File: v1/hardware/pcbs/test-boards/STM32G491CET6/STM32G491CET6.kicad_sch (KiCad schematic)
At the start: 43 parts, among them J1 Conn_02x10_Odd_Even, J2 Conn_02x10_Odd_Even, J3 Conn_01x04, U1 STM32G491CETx, Y1 Crystal_GND24, Y2 Crystal

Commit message: not sure what i did
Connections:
- net +3V3: now also C6.2, U1.1 (VBAT)
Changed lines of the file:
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@@
 	)
 	(junction
+		(at 107.95 54.61)
+		(diameter 0)
+		(color 0 0 0 0)
+	)
+	(junction
 		(at 157.48 54.61)
 		(diameter 0)
@@
 					(unit 1)
 				)
+			)
+		)
+	)
+	(symbol
+		(lib_id "power:+3V3")
+		(at 107.95 54.61 90)
+		(unit 1)
+		(exclude_from_sim no)
+		(in_bom yes)
+		(on_board yes)
+		(dnp no)
+		(fields_autoplaced yes)
+		(property "Reference" "#PWR057"
+			(at 111.76 54.61 0)
+			(effects
+				(font
+					(size 1.27 1.27)
+				)
+				(hide yes)
+			)
+		)
+		(property "Value" "+3V3"
+			(at 104.14 54.61 90)
+			(effects
+				(font
+					(size 1.27 1.27)
+				)
+				(justify left)
+			)
+		)
+		(property "Footprint" ""
+			(at 107.95 54.61 0)
+			(effects
+				(font
+					(size 1.27 1.27)
+				)
+				(hide yes)
+			)
+		)
+		(property "Datasheet" ""
+			(at 107.95 54.61 0)
+			(effects
+				(font
+					(size 1.27 1.27)
+				)
+				(hide yes)
+			)
+		)
+		(property "Description" "Power symbol creates a global label with name \"+3V3\""
+			(at 107.95 54.61 0)
+			(effects
+				(font
+					(size 1.27 1.27)
+				)
+				(hide yes)
+			)
+		)
+		(pin "1"
+		)
+		(instances
+			(project "STM32G491CET6"
+				(path "/ca218c03-4ff0-46e7-9492-03c917b647a9"
+					(reference "#PWR057")
+					(unit 1)
+				)

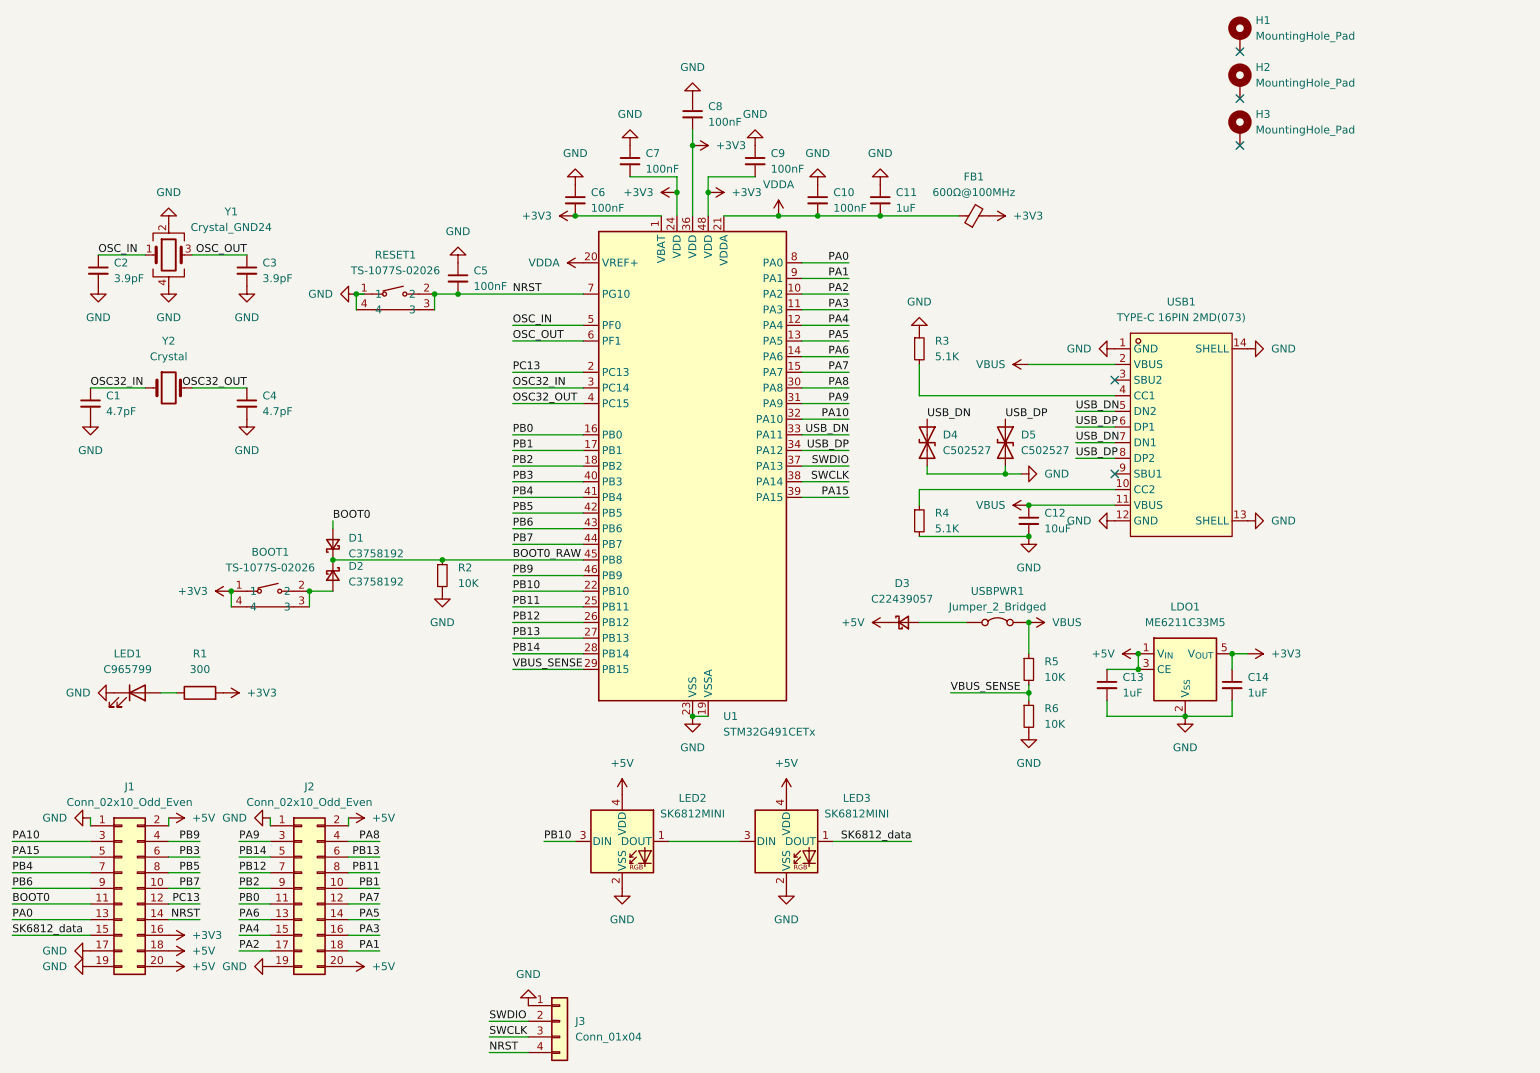
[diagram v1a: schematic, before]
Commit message: fixed STM32G4 breakout board boot pin floating, and changed RGB LEDs to indicator LED
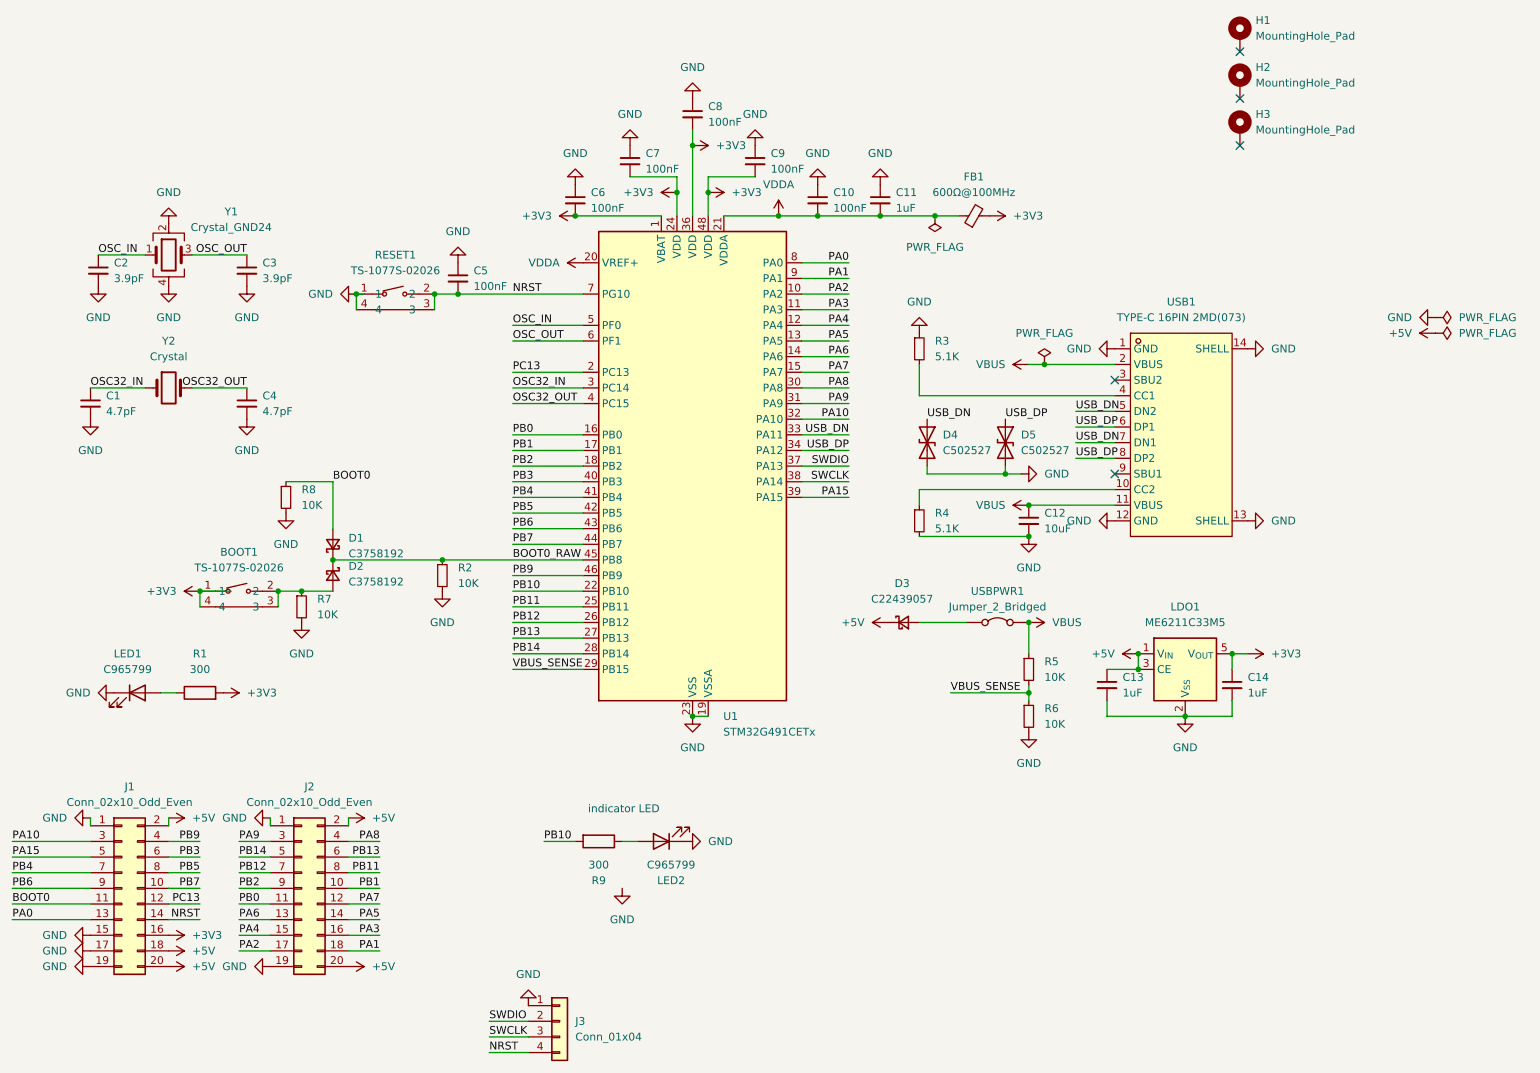
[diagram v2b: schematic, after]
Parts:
- removed LED2, LED3: SK6812MINI, LED_SMD:LED_SK6812MINI_PLCC4_3.5x3.5mm_P1.75mm, symbol LED:SK6812MINI
- added LED2: C965799, LED_SMD:LED_0603_1608Metric, symbol Device:LED
- added R7, R8: 10K, Resistor_SMD:R_0603_1608Metric, symbol Device:R_Small
- added R9: 300, Resistor_SMD:R_0603_1608Metric, symbol Device:R
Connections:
- net SK6812_data is gone; now on net GND: J1.15 (Pin_15)
- net BOOT0: now also R8.1
- net GND: now also LED2.1 (K), R7.2, R8.2
- net PB10: now also R9.2
- net at BOOT1.2, BOOT1.3, D2.2 (A): now also R7.1
- new net: LED2.2 (A), R9.1
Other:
- note added: "indicator LED"
- moved on the sheet: BOOT1
